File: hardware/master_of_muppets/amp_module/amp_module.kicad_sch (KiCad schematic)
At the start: 21 parts

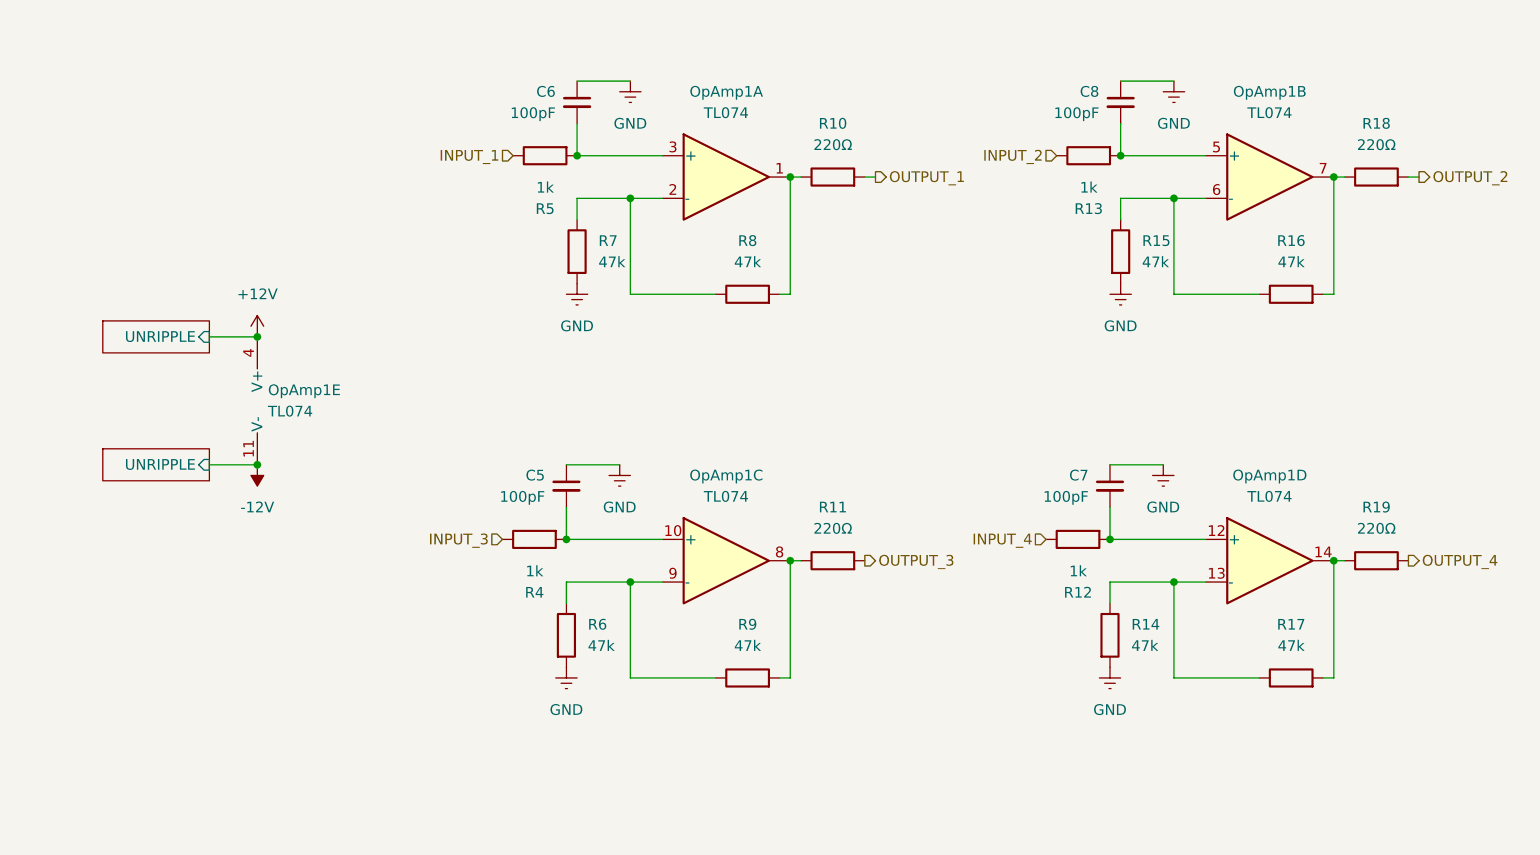
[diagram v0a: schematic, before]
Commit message: Making the boards truly hierarchical using projectinstances plugin
https://github.com/OfficialDyray/projectinstances
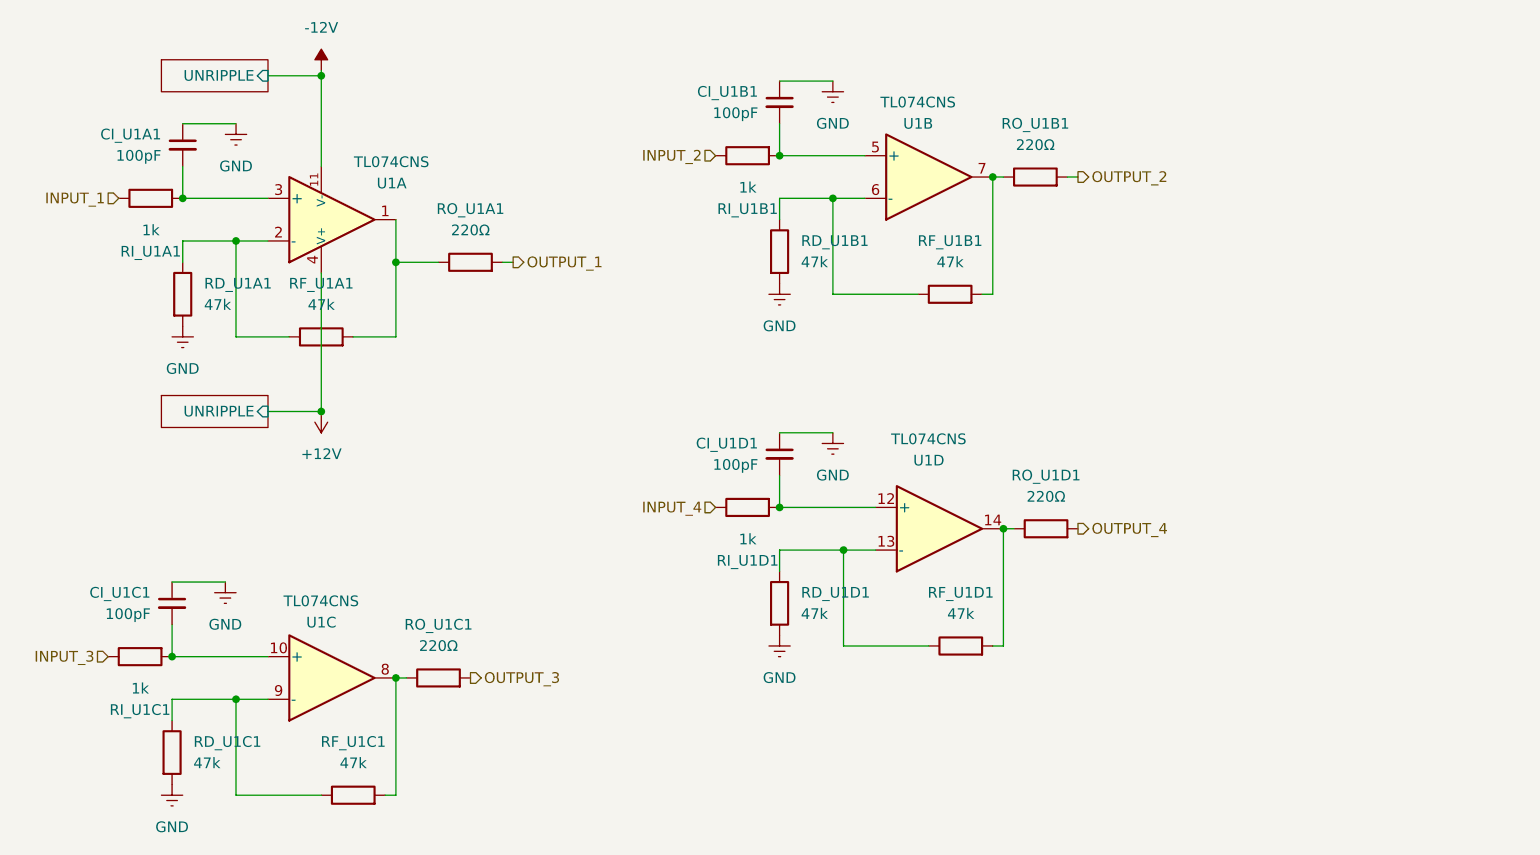
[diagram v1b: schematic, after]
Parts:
- removed OpAmp1: TL074, Package_SO:SOIC-14_3.9x8.7mm_P1.27mm, symbol Amplifier_Operational:TL074
- added U1: TL074CNS, PCM_Package_SO_AKL:SO-14_5.3x10.2mm_P1.27mm, symbol PCM_Amplifier_Operational_AKL:TL074CNS
- renumbered C6 to CI_U1A1, C8 to CI_U1B1, C5 to CI_U1C1, C7 to CI_U1D1, R7 to RD_U1A1, R15 to RD_U1B1, R6 to RD_U1C1, R14 to RD_U1D1, R8 to RF_U1A1, R16 to RF_U1B1, R9 to RF_U1C1, R17 to RF_U1D1, R5 to RI_U1A1, R13 to RI_U1B1, R4 to RI_U1C1, R12 to RI_U1D1, R10 to RO_U1A1, R18 to RO_U1B1, R11 to RO_U1C1, R19 to RO_U1D1
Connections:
- net +12V: now also U1.4 (V+)
- net -12V: now also U1.11 (V-)
- net at RF_U1B1.2, RO_U1B1.1: now also U1.7
- net at CI_U1B1.2, RI_U1B1.2: now also U1.5 (+)
- net at CI_U1D1.2, RI_U1D1.2: now also U1.12 (+)
- net at RD_U1B1.1, RF_U1B1.1: now also U1.6 (-)
- net at RD_U1C1.1, RF_U1C1.1: now also U1.9 (-)
- net at CI_U1A1.2, RI_U1A1.2: now also U1.3 (+)
- net at RF_U1D1.2, RO_U1D1.1: now also U1.14
- net at RD_U1A1.1, RF_U1A1.1: now also U1.2 (-)
- net at RF_U1C1.2, RO_U1C1.1: now also U1.8
- net at CI_U1C1.2, RI_U1C1.2: now also U1.10 (+)
- net at RD_U1D1.1, RF_U1D1.1: now also U1.13 (-)
- net at RF_U1A1.2, RO_U1A1.1: now also U1.1
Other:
- sheet UNRIPPLE_MODULE1: file unripple_module.kicad_sch -> ../unripple_module/unripple_module.kicad_sch
- sheet UNRIPPLE_MODULE2: file unripple_module.kicad_sch -> ../unripple_module/unripple_module.kicad_sch
- moved on the sheet: CI_U1A1, CI_U1B1, CI_U1C1, CI_U1D1, RD_U1A1, RD_U1B1, RD_U1C1, RD_U1D1, RF_U1A1, RF_U1B1, RF_U1C1, RF_U1D1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
